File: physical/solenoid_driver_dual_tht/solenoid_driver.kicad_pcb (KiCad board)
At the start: 2 copper layers, 53 x 57 mm, 41 parts, among them J1 Input, J2 Solenoid B Override, J3 Solenoid A Override, J4 SenseA, J5 Solenoid A, J6 SenseB, J7 Solenoid B, J8 12V Input, Q1 TIP120, Q2 TIP120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

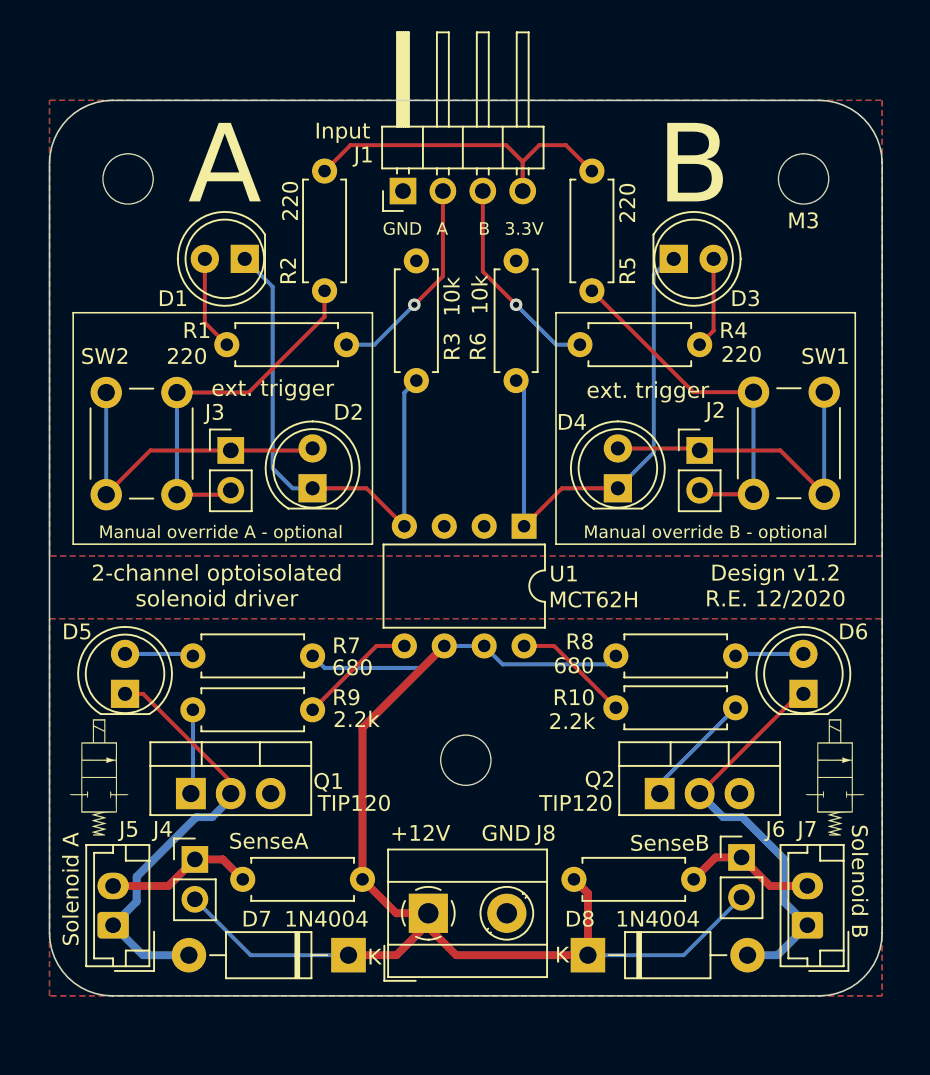
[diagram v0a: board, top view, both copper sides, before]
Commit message: Dual THT solenoid PCB updates
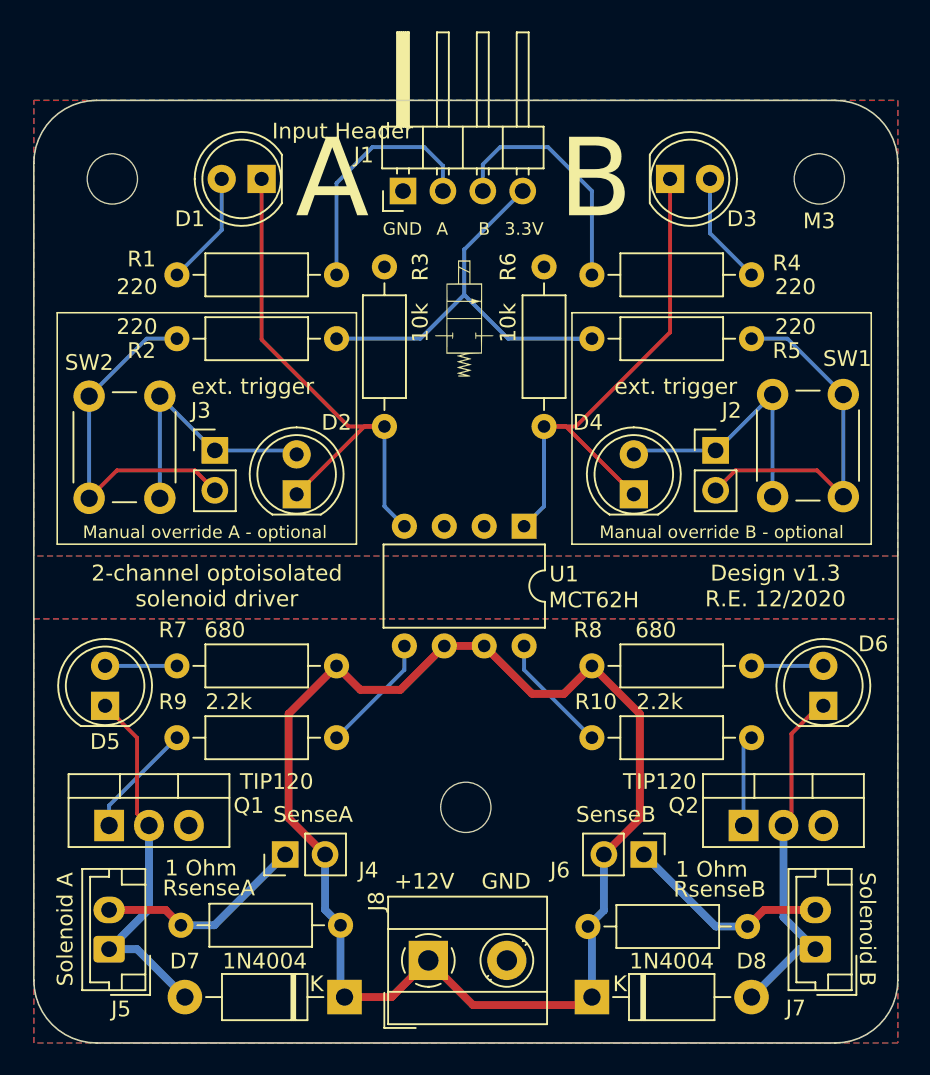
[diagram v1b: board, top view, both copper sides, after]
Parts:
- removed the G*** at (113.2, 102.1)
- J1: value Input -> Input Header
- R1, R10, R2, R3, R4, R5, R6, R7, R8, R9: footprint Resistor_THT:R_Axial_DIN0207_L6.3mm_D2.5mm_P7.62mm_Horizontal -> Resistor_THT:R_Axial_DIN0207_L6.3mm_D2.5mm_P10.16mm_Horizontal
- RsenseA: renamed from RsenseA1; value 1 -> 1 Ohm; footprint Resistor_THT:R_Axial_DIN0207_L6.3mm_D2.5mm_P7.62mm_Horizontal -> Resistor_THT:R_Axial_DIN0207_L6.3mm_D2.5mm_P10.16mm_Horizontal
- RsenseB: renamed from RsenseB1; value 1 -> 1 Ohm; footprint Resistor_THT:R_Axial_DIN0207_L6.3mm_D2.5mm_P7.62mm_Horizontal -> Resistor_THT:R_Axial_DIN0207_L6.3mm_D2.5mm_P10.16mm_Horizontal
- moved G*** 37.6 mm to (136.4, 72.9)
- moved G*** 33.1 mm to (123.0, 74.5) (x2)
- moved R5 10.6 mm to (154.7, 74.2), turned to 180 degrees
- moved R2 9.88 mm to (118.1, 74.2), turned to 0 degrees
- moved SW2 8.75 mm to (112.5, 84.3), turned to 90 degrees
- moved SW1 8.54 mm to (160.5, 77.7), turned to 270 degrees
- moved J6 6.23 mm to (147.8, 107.0), turned to 270 degrees
- moved J4 5.76 mm to (125.0, 107.0), turned to 90 degrees
- moved Q2 5.71 mm to (154.2, 105.2)
- moved Q1 5.59 mm to (113.8, 105.2)
- moved R4 5.54 mm to (154.7, 70.1)
- moved R1 5.46 mm to (118.1, 70.1)
- moved D1 5.20 mm to (123.5, 64.0)
- moved D3 5.09 mm to (149.5, 64.0)
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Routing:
- net 3.3V: track 21.1 -> 27.8 mm
- net Net-(J6-Pad1): track 8.57 -> 13.3 mm
- net Net-(J4-Pad1): track 9.48 -> 13.5 mm
- net Net-(D5-Pad1): track 27.8 -> 23.8 mm
- net Net-(D4-Pad2): track 20.8 -> 17.3 mm
- net Net-(D6-Pad1): track 26.5 -> 23.0 mm
- net 12V: track 89.1 -> 85.8 mm
- net Net-(D2-Pad2): track 20.9 -> 17.6 mm
- net InputB: track 13.2 -> 15.6 mm, vias 1 -> 0
- net InputA: track 13.4 -> 15.7 mm, vias 1 -> 0
- net Net-(Q1-Pad1): track 5.39 -> 7.38 mm
- net Net-(Q2-Pad1): track 7.46 -> 5.80 mm
- net Net-(D3-Pad2): track 5.83 -> 7.20 mm
- net Net-(D3-Pad1): track 33.4 -> 34.6 mm
- net Net-(D1-Pad2): track 6.04 -> 7.28 mm
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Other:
- board size 53 x 57 mm -> 55 x 60 mm
- board text added: "Design v1.3 R.E. 12/2020"
- board text removed: "Design v1.2 R.E. 12/2020"
